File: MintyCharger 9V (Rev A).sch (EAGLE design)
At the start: 32 parts, among them IC1 PIC12F683P, IC2 7805L, IC3 LM358N, Q1 2N3904, Q2 2N3904, Q3 BD139

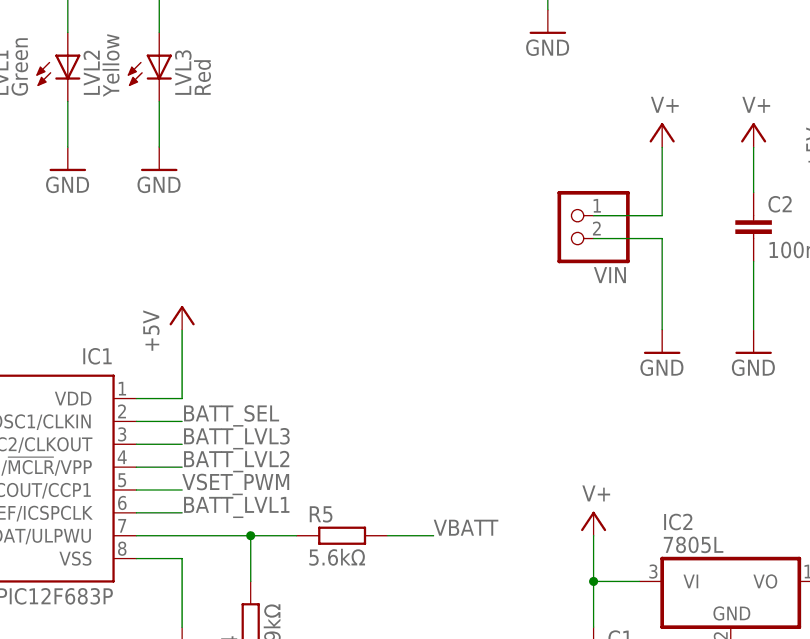
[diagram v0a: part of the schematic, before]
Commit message: Moved BATT_SEL to GP3
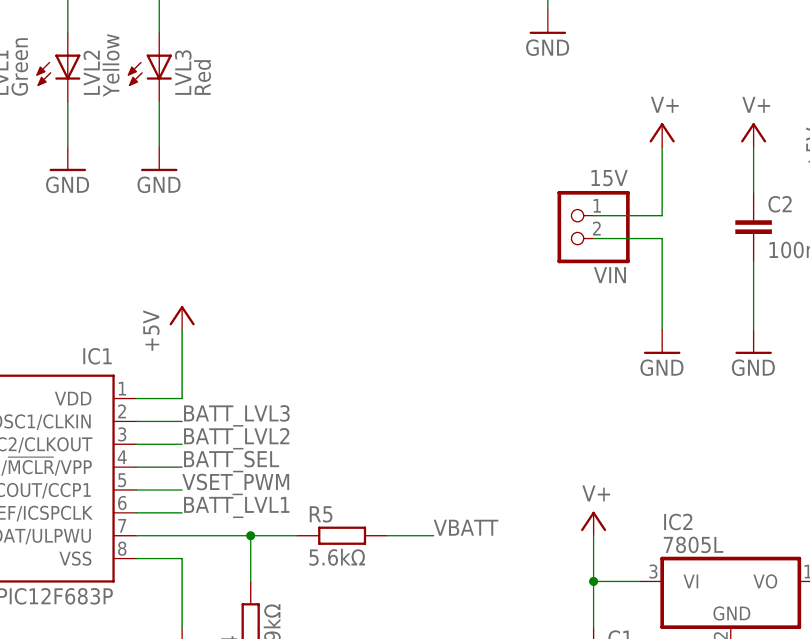
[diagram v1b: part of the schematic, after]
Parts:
- VIN: value (none) -> 15V
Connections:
- net BATT_LVL2: now also IC1.GP4/AN3/T1G/OSC2/CLKOUT; no longer IC1.GP3/!MCLR!/VPP
- net BATT_LVL3: now also IC1.GP5/T1CKI/OSC1/CLKIN; no longer IC1.GP4/AN3/T1G/OSC2/CLKOUT
- net BATT_SEL: now also IC1.GP3/!MCLR!/VPP; no longer IC1.GP5/T1CKI/OSC1/CLKIN
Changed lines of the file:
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@@
 <part name="GND19" library="supply1" deviceset="GND" device=""/>
 <part name="BATT" library="adafruit" deviceset="JST_2PIN" device="-THM"/>
-<part name="VIN" library="adafruit" deviceset="JST_2PIN" device="-THM"/>
+<part name="VIN" library="adafruit" deviceset="JST_2PIN" device="-THM" value="15V"/>
 <part name="P+6" library="supply1" deviceset="+5V" device=""/>
 <part name="D2" library="diode" deviceset="1N4148" device="DO35-7"/>
@@
 </segment>
 <segment>
-<pinref part="IC1" gate="G$1" pin="GP5/T1CKI/OSC1/CLKIN"/>
-<wire x1="48.26" y1="45.72" x2="53.34" y2="45.72" width="0.1524" layer="91"/>
-<label x="53.34" y="45.72" size="1.778" layer="95"/>
+<pinref part="IC1" gate="G$1" pin="GP3/!MCLR!/VPP"/>
+<wire x1="48.26" y1="40.64" x2="53.34" y2="40.64" width="0.1524" layer="91"/>
+<label x="53.34" y="40.64" size="1.778" layer="95"/>
 </segment>
 </net>
@@
 </segment>
 <segment>
-<pinref part="IC1" gate="G$1" pin="GP3/!MCLR!/VPP"/>
-<wire x1="48.26" y1="40.64" x2="53.34" y2="40.64" width="0.1524" layer="91"/>
-<label x="53.34" y="40.64" size="1.778" layer="95"/>
+<pinref part="IC1" gate="G$1" pin="GP4/AN3/T1G/OSC2/CLKOUT"/>
+<wire x1="48.26" y1="43.18" x2="53.34" y2="43.18" width="0.1524" layer="91"/>
+<label x="53.34" y="43.18" size="1.778" layer="95"/>
 </segment>
 </net>
@@
 </segment>
 <segment>
-<pinref part="IC1" gate="G$1" pin="GP4/AN3/T1G/OSC2/CLKOUT"/>
-<wire x1="48.26" y1="43.18" x2="53.34" y2="43.18" width="0.1524" layer="91"/>
-<label x="53.34" y="43.18" size="1.778" layer="95"/>
-</segment>
-</net>
+<pinref part="IC1" gate="G$1" pin="GP5/T1CKI/OSC1/CLKIN"/>
+<wire x1="48.26" y1="45.72" x2="53.34" y2="45.72" width="0.1524" layer="91"/>
+<label x="53.34" y="45.72" size="1.778" layer="95"/>
+</segment>
+</net>
